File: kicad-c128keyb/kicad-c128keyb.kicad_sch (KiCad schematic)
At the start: 19 parts, among them J1 KBD_FLAT26, J2 DB25_Male_MountingHoles, J3 OLED_128x32, J4 EXT_POWER_5V, Q1 2N3904, Q2 2N3904, Q3 2N3904, U1 MT8816, U2 74HC595, U3 SeeeduinoXIAO

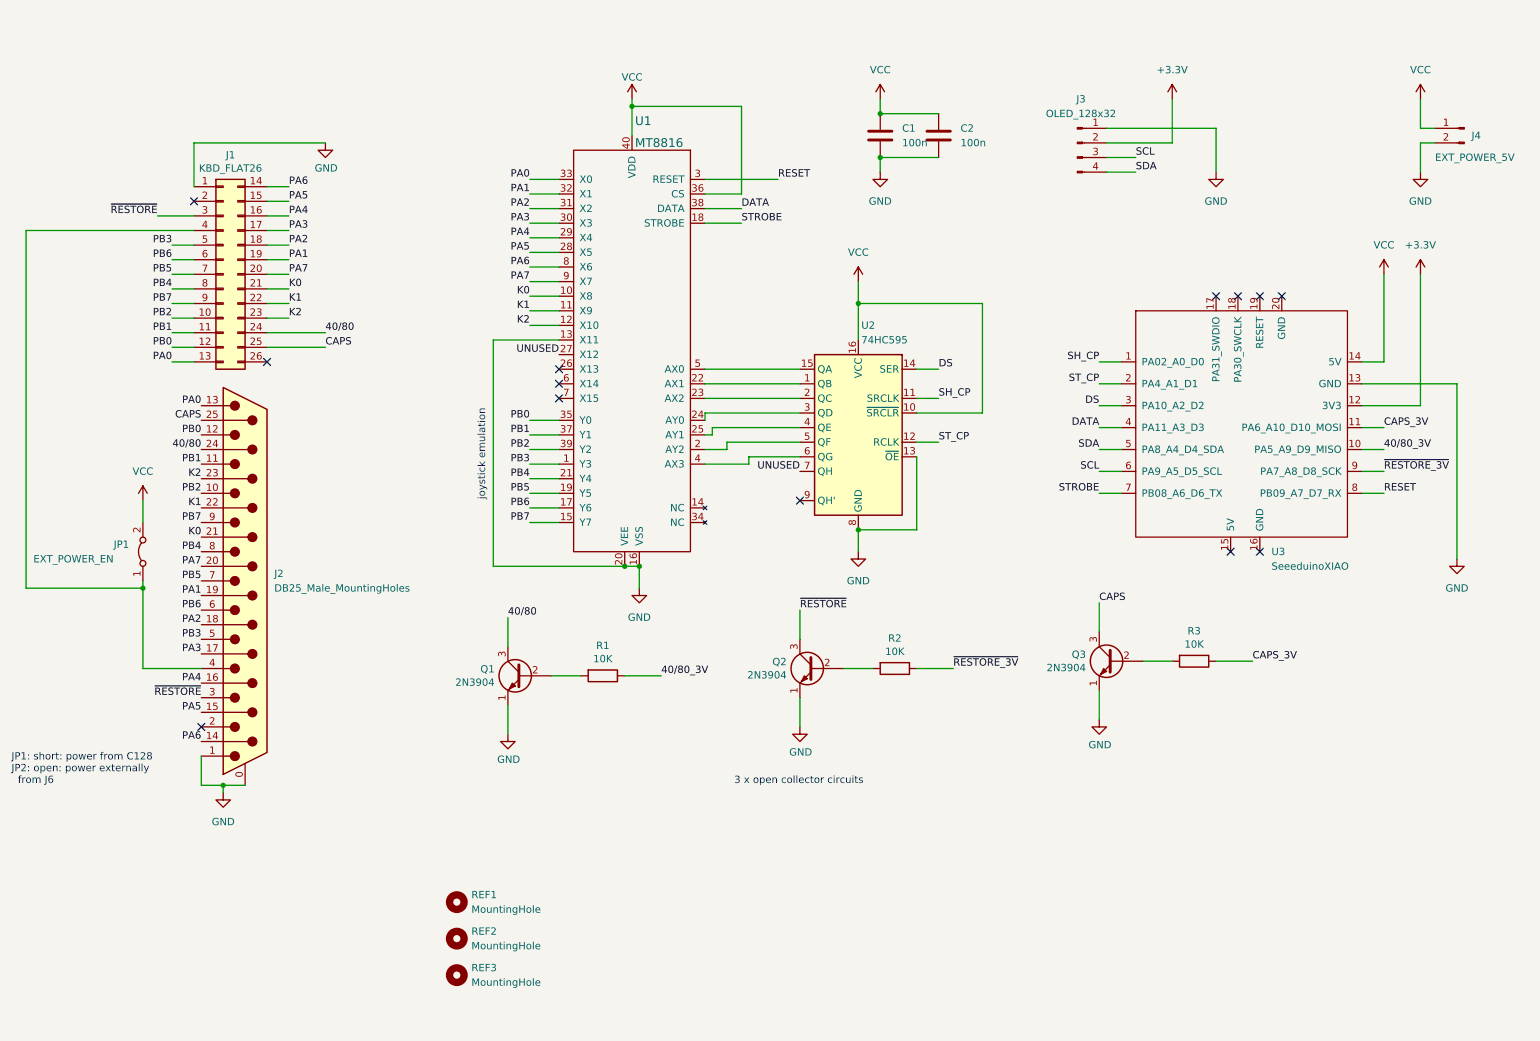
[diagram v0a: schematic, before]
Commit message: common C16/C64 version for internal mount; despite filenames this is not about C128 anymore; downgraded from MT8816 to MT8808
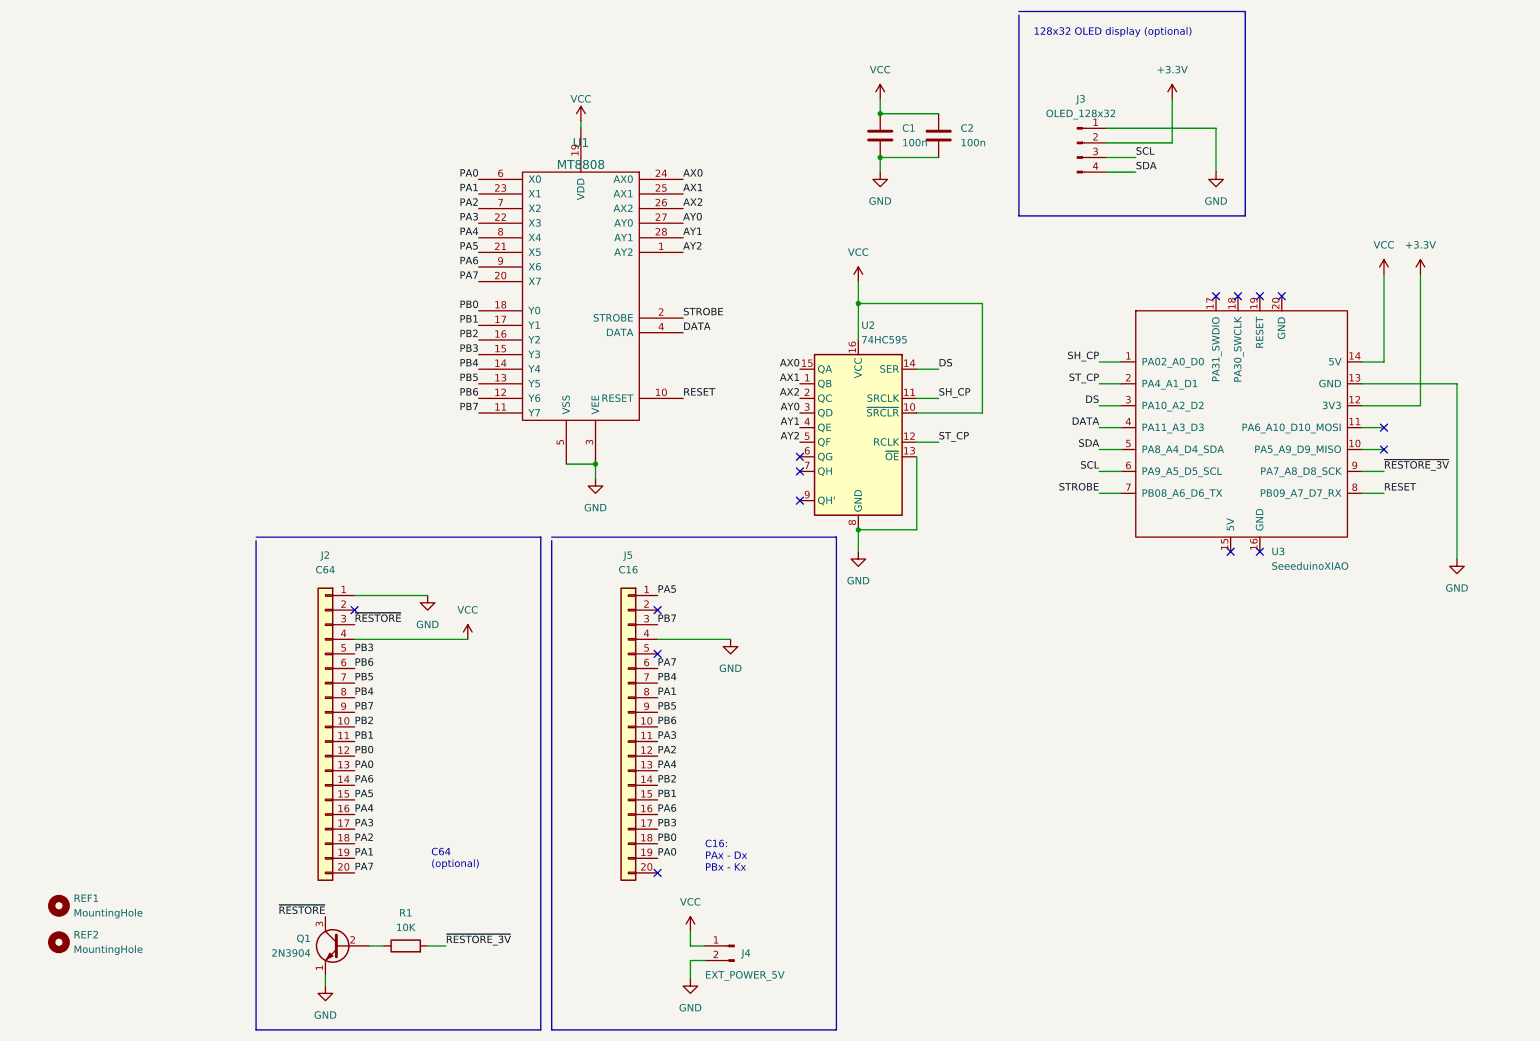
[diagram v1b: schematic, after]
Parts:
- removed J1: KBD_FLAT26, Connector_PinHeader_2.54mm:PinHeader_2x13_P2.54mm_Vertical, symbol Connector_Generic:Conn_02x13_Top_Bottom
- removed J2: DB25_Male_MountingHoles, Connector_Dsub:DSUB-25_Male_Horizontal_P2.77x2.84mm_EdgePinOffset4.94mm_Housed_MountingHolesOffset7.48mm, symbol Connector:DB25_Male_MountingHoles
- removed JP1: EXT_POWER_EN, Connector_PinHeader_2.54mm:PinHeader_1x02_P2.54mm_Vertical, symbol Jumper:Jumper_2_Bridged
- removed Q2, Q3: 2N3904, Package_TO_SOT_THT:TO-92_Inline, symbol Transistor_BJT:2N3904
- removed R2, R3: 10K, Resistor_THT:R_Axial_DIN0207_L6.3mm_D2.5mm_P7.62mm_Horizontal, symbol Device:R
- removed REF3: MountingHole, MountingHole:MountingHole_2.2mm_M2_Pad_Via, symbol Mechanical:MountingHole
- removed U1: MT8816, Package_DIP:DIP-40_W15.24mm_Socket, symbol mt8808:MT8816
- added J2: C64, Connector_PinHeader_2.54mm:PinHeader_1x20_P2.54mm_Vertical, symbol Connector_Generic:Conn_01x20
- added J5: C16, Connector_PinHeader_2.54mm:PinHeader_1x20_P2.54mm_Vertical, symbol Connector_Generic:Conn_01x20
- added U1: MT8808, Package_DIP:DIP-28_W15.24mm_Socket, symbol mt8808:MT8808
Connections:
- net 40/80 is gone; now on net ~{RESTORE}: Q1.3 (C)
- net DATA: now also U1.4 (DATA)
- net GND: now also J2.1 (Pin_1), J5.4 (Pin_4), U1.3 (VEE), U1.5 (VSS)
- net PA0: now also J2.13 (Pin_13), J5.19 (Pin_19), U1.6 (X0)
- net PA1: now also J2.19 (Pin_19), J5.8 (Pin_8), U1.23 (X1)
- net PA2: now also J2.18 (Pin_18), J5.12 (Pin_12), U1.7 (X2)
- net PA3: now also J2.17 (Pin_17), J5.11 (Pin_11), U1.22 (X3)
- net PA4: now also J2.16 (Pin_16), J5.13 (Pin_13), U1.8 (X4)
- net PA5: now also J2.15 (Pin_15), J5.1 (Pin_1), U1.21 (X5)
- net PA6: now also J2.14 (Pin_14), J5.16 (Pin_16), U1.9 (X6)
- net PA7: now also J2.20 (Pin_20), J5.6 (Pin_6), U1.20 (X7)
- net PB0: now also J2.12 (Pin_12), J5.18 (Pin_18), U1.18 (Y0)
- net PB1: now also J2.11 (Pin_11), J5.15 (Pin_15), U1.17 (Y1)
- net PB2: now also J2.10 (Pin_10), J5.14 (Pin_14), U1.16 (Y2)
- net PB3: now also J2.5 (Pin_5), J5.17 (Pin_17), U1.15 (Y3)
- net PB4: now also J2.8 (Pin_8), J5.7 (Pin_7), U1.14 (Y4)
- net PB5: now also J2.7 (Pin_7), J5.9 (Pin_9), U1.13 (Y5)
- net PB6: now also J2.6 (Pin_6), J5.10 (Pin_10), U1.12 (Y6)
- net PB7: now also J2.9 (Pin_9), J5.3 (Pin_3), U1.11 (Y7)
- net RESET: now also U1.10 (RESET)
- net STROBE: now also U1.2 (STROBE)
- net VCC: now also J2.4 (Pin_4), U1.19 (VDD)
- net ~{RESTORE_3V}: now also R1.2
- net ~{RESTORE}: now also J2.3 (Pin_3)
- net at Q1.2 (B): now also R1.1; no longer R1.2
- net AX1: now reaches U2.1 (QB)
- net AX1: now also U1.25 (AX1)
- net AX0: now reaches U2.15 (QA)
- net AX0: now also U1.24 (AX0)
- net AX2: now reaches U2.2 (QC)
- net AX2: now also U1.26 (AX2)
- net AY0: now reaches U2.3 (QD)
- net AY0: now also U1.27 (AY0)
- net AY1: now reaches U2.4 (QE)
- net AY1: now also U1.28 (AY1)
- net AY2: now reaches U2.5 (QF)
- net AY2: now also U1.1 (AY2)
- net 40/80_3V: no longer names the net of U3.10 (PA5_A9_D9_MISO)
- net 40/80_3V: no longer R1.1
- net CAPS_3V: no longer names the net of U3.11 (PA6_A10_D10_MOSI)
- net UNUSED: no longer names the net of U2.7 (QH)
- no-connect marks 13 -> 15
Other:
- note added: "128x32 OLED display (optional)"
- note added: "C16: PAx - Dx PBx - Kx"
- note added: "C64 (optional)"
- note removed: "3 x open collector circuits"
- note removed: "JP1: short: power from C128 JP2: open: power externally from J6"
- note removed: "joystick emulation"
- title: SEEDUINO C128 Keyboard Adapter -> SEEDUINO C16/64 Keyboard Adapter
- moved on the sheet: J4, REF1, REF2
